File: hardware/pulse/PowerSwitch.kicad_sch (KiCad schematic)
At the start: 22 parts, among them J1801 WAGO 2065-100, J1802 WAGO 2065-100, U1801 BTT6010

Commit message: Refresh
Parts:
- U1801: Rating (none) -> 36V
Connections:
- net +24V-Supply renamed +28V-Supply
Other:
- note added: "100R / Solenoid coil voltage divider Supplies reference voltage to a single channel while the +28V power is switched off."
- note removed: "100R / Solenoid coil voltage divider Supplies reference voltage to a single channel while the +24V power is switched off."
- company: +24V -> Versio Duo
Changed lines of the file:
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@@
 	(title_block
 		(title "Power Switch")
-		(date "2023-01-07")
-		(rev "1")
-		(company "+24V")
-		(comment 1 "Voltage + Current Sense")
+		(date "2026-02-24")
+		(rev "2026-02-24")
+		(company "Versio Duo")
+		(comment 1 "+28V")
+		(comment 2 "Voltage + Current Sense")
 	)
 	(text "Supply Voltage"
@@
 		)
 	)
-	(text "100R / Solenoid coil voltage divider\nSupplies reference voltage to a single channel\nwhile the +24V power is switched off."
+	(text "100R / Solenoid coil voltage divider\nSupplies reference voltage to a single channel\nwhile the +28V power is switched off."
 		(exclude_from_sim no)
 		(at 180.34 149.225 0)
@@
 		)
 	)
-	(label "+24V-Supply"
+	(label "+28V-Supply"
 		(at 177.8 68.58 0)
 		(effects
@@
 		)
 	)
-	(label "+24V-Supply"
+	(label "+28V-Supply"
 		(at 101.6 120.65 0)
 		(effects
@@
 		)
 	)
-	(label "+24V-Supply"
+	(label "+28V-Supply"
 		(at 156.21 76.2 180)
 		(effects
@@
 		)
 	)
-	(label "+24V-Supply"
+	(label "+28V-Supply"
 		(at 128.27 68.58 180)
 		(effects
@@
 		(on_board yes)
 		(dnp no)
-		(property "Reference" "#PWR01805"
+		(property "Reference" "#PWR1805"
 			(at 102.87 90.17 0)
 			(effects
@@
 			(project "pulse"
 				(path "/6c8448b4-b04d-47e1-934e-e40cbe27a7be/ba748654-beb9-4861-aa35-c19e08caaf2e"
-					(reference "#PWR01805")
+					(reference "#PWR1805")
 					(unit 1)
 				)
@@
 		(on_board yes)
 		(dnp no)
-		(property "Reference" "#PWR01804"
+		(property "Reference" "#PWR1804"
 			(at 218.44 87.63 0)
 			(effects
@@
 			(project "pulse"
 				(path "/6c8448b4-b04d-47e1-934e-e40cbe27a7be/ba748654-beb9-4861-aa35-c19e08caaf2e"
-					(reference "#PWR01804")
+					(reference "#PWR1804")
 					(unit 1)
 				)
@@
 		(on_board yes)
 		(dnp no)
-		(property "Reference" "#PWR01802"
+		(property "Reference" "#PWR1802"
 			(at 132.08 87.63 0)
 			(effects
@@
 			(project "pulse"
 				(path "/6c8448b4-b04d-47e1-934e-e40cbe27a7be/ba748654-beb9-4861-aa35-c19e08caaf2e"
-					(reference "#PWR01802")
+					(reference "#PWR1802")
 					(unit 1)
 				)
@@
 		(on_board yes)
 		(dnp no)
-		(property "Reference" "#PWR01817"
+		(property "Reference" "#PWR1817"
 			(at 107.95 147.32 0)
 			(effects
@@
 			(project "pulse"
 				(path "/6c8448b4-b04d-47e1-934e-e40cbe27a7be/ba748654-beb9-4861-aa35-c19e08caaf2e"
-					(reference "#PWR01817")
+					(reference "#PWR1817")
 					(unit 1)
 				)
@@
 		(on_board yes)
 		(dnp no)
-		(property "Reference" "#PWR01809"
+		(property "Reference" "#PWR1809"
 			(at 154.94 132.08 0)
 			(effects
@@
 			(project "pulse"
 				(path "/6c8448b4-b04d-47e1-934e-e40cbe27a7be/ba748654-beb9-4861-aa35-c19e08caaf2e"
-					(reference "#PWR01809")
+					(reference "#PWR1809")
 					(unit 1)
 				)
@@
 		(on_board yes)
 		(dnp no)
-		(property "Reference" "#PWR01811"
+		(property "Reference" "#PWR1811"
 			(at 85.09 137.16 0)
 			(effects
@@
 			(project "pulse"
 				(path "/6c8448b4-b04d-47e1-934e-e40cbe27a7be/ba748654-beb9-4861-aa35-c19e08caaf2e"
-					(reference "#PWR01811")
+					(reference "#PWR1811")
 					(unit 1)
 				)
@@
 		(on_board yes)
 		(dnp no)
-		(property "Reference" "#PWR01814"
+		(property "Reference" "#PWR1814"
 			(at 217.17 137.16 0)
 			(effects
@@
 			(project "pulse"
 				(path "/6c8448b4-b04d-47e1-934e-e40cbe27a7be/ba748654-beb9-4861-aa35-c19e08caaf2e"
-					(reference "#PWR01814")
+					(reference "#PWR1814")
 					(unit 1)
 				)
@@
 		(on_board yes)
 		(dnp no)
-		(property "Reference" "#PWR01807"
+		(property "Reference" "#PWR1807"
 			(at 199.39 124.46 0)
 			(effects
@@
 			(project "pulse"
 				(path "/6c8448b4-b04d-47e1-934e-e40cbe27a7be/ba748654-beb9-4861-aa35-c19e08caaf2e"
-					(reference "#PWR01807")
+					(reference "#PWR1807")
 					(unit 1)
 				)
@@
 		(on_board yes)
 		(dnp no)
-		(property "Reference" "#PWR01815"
+		(property "Reference" "#PWR1815"
 			(at 143.51 135.89 0)
 			(effects
@@
 			(project "pulse"
 				(path "/6c8448b4-b04d-47e1-934e-e40cbe27a7be/ba748654-beb9-4861-aa35-c19e08caaf2e"
-					(reference "#PWR01815")
+					(reference "#PWR1815")
 					(unit 1)
 				)
@@
 		(on_board yes)
 		(dnp no)
-		(property "Reference" "#PWR01801"
+		(property "Reference" "#PWR1801"
 			(at 120.65 87.63 0)
 			(effects
@@
 			(project "pulse"
 				(path "/6c8448b4-b04d-47e1-934e-e40cbe27a7be/ba748654-beb9-4861-aa35-c19e08caaf2e"
-					(reference "#PWR01801")
+					(reference "#PWR1801")
 					(unit 1)
 				)
@@
 			)
 		)
-		(property "Description" "Infineon Smart High Sde Switches PROFET™+ 24V"
+		(property "Description" "Infineon Smart High Side Switches PROFET™+ 24V"
 			(at 127 128.27 0)
 			(effects
@@
 			)
 		)
+		(property "Rating" "36V"
+			(at 127 179.07 0)
+			(effects
+				(font
+					(size 1.27 1.27)
+				)
+				(hide yes)
+			)
+		)
 		(pin "1"
 		)
@@
 		(on_board yes)
 		(dnp no)
-		(property "Reference" "#PWR01806"
+		(property "Reference" "#PWR1806"
 			(at 167.64 124.46 0)
 			(effects
@@
 			(project "pulse"
 				(path "/6c8448b4-b04d-47e1-934e-e40cbe27a7be/ba748654-beb9-4861-aa35-c19e08caaf2e"
-					(reference "#PWR01806")
+					(reference "#PWR1806")
 					(unit 1)
 				)
@@
 		(on_board yes)
 		(dnp no)
-		(property "Reference" "#PWR01813"
+		(property "Reference" "#PWR1813"
 			(at 199.39 127 0)
 			(effects
@@
 			(project "pulse"
 				(path "/6c8448b4-b04d-47e1-934e-e40cbe27a7be/ba748654-beb9-4861-aa35-c19e08caaf2e"
-					(reference "#PWR01813")
+					(reference "#PWR1813")
 					(unit 1)
 				)
@@
 		(on_board yes)
 		(dnp no)
-		(property "Reference" "#PWR01818"
+		(property "Reference" "#PWR1818"
 			(at 116.84 147.32 0)
 			(effects
@@
 			(project "pulse"
 				(path "/6c8448b4-b04d-47e1-934e-e40cbe27a7be/ba748654-beb9-4861-aa35-c19e08caaf2e"
-					(reference "#PWR01818")
+					(reference "#PWR1818")
 					(unit 1)
 				)
@@
 		(on_board yes)
 		(dnp no)
-		(property "Reference" "#PWR01803"
+		(property "Reference" "#PWR1803"
 			(at 193.04 87.63 0)
 			(effects
@@
 			(project "pulse"
 				(path "/6c8448b4-b04d-47e1-934e-e40cbe27a7be/ba748654-beb9-4861-aa35-c19e08caaf2e"
-					(reference "#PWR01803")
+					(reference "#PWR1803")
 					(unit 1)
 				)
@@
 		(on_board yes)
 		(dnp no)
-		(property "Reference" "#PWR01810"
+		(property "Reference" "#PWR1810"
 			(at 167.64 132.08 0)
 			(effects
@@
 			(project "pulse"
 				(path "/6c8448b4-b04d-47e1-934e-e40cbe27a7be/ba748654-beb9-4861-aa35-c19e08caaf2e"
-					(reference "#PWR01810")
+					(reference "#PWR1810")
 					(unit 1)
 				)
@@
 		(on_board yes)
 		(dnp no)
-		(property "Reference" "#FLG01801"
+		(property "Reference" "#FLG1801"
 			(at 113.03 66.675 0)
 			(effects
@@
 			(project "pulse"
 				(path "/6c8448b4-b04d-47e1-934e-e40cbe27a7be/ba748654-beb9-4861-aa35-c19e08caaf2e"
-					(reference "#FLG01801")
+					(reference "#FLG1801")
 					(unit 1)
 				)
@@
 		(on_board yes)
 		(dnp no)
-		(property "Reference" "#PWR01808"
+		(property "Reference" "#PWR1808"
 			(at 142.24 132.08 0)
 			(effects
@@
 			(project "pulse"
 				(path "/6c8448b4-b04d-47e1-934e-e40cbe27a7be/ba748654-beb9-4861-aa35-c19e08caaf2e"
-					(reference "#PWR01808")
+					(reference "#PWR1808")
 					(unit 1)
 				)
@@
 		(on_board yes)
 		(dnp no)
-		(property "Reference" "#PWR01816"
+		(property "Reference" "#PWR1816"
 			(at 85.09 147.32 0)
 			(effects
@@
 			(project "pulse"
 				(path "/6c8448b4-b04d-47e1-934e-e40cbe27a7be/ba748654-beb9-4861-aa35-c19e08caaf2e"
-					(reference "#PWR01816")
+					(reference "#PWR1816")
 					(unit 1)
 				)
@@
 		(on_board yes)
 		(dnp no)
-		(property "Reference" "#PWR01812"
+		(property "Reference" "#PWR1812"
 			(at 120.65 130.81 0)
 			(effects
@@
 			(project "pulse"
 				(path "/6c8448b4-b04d-47e1-934e-e40cbe27a7be/ba748654-beb9-4861-aa35-c19e08caaf2e"
-					(reference "#PWR01812")
+					(reference "#PWR1812")
 					(unit 1)
 				)

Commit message: Refresh
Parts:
- C1801: Mouser 810-CNA6P1X7R1H106K2 -> 810-CNC6P1X7R1H106K2; Product CNA6P1X7R1H106K250AE -> CNC6P1X7R1H106K250AE
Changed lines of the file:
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@@
 			)
 		)
-		(property "Mouser" "810-CNA6P1X7R1H106K2"
+		(property "Mouser" "810-CNC6P1X7R1H106K2"
 			(at 120.65 95.25 0)
 			(show_name yes)
@@
 			)
 		)
-		(property "Product" "CNA6P1X7R1H106K250AE"
+		(property "Product" "CNC6P1X7R1H106K250AE"
 			(at 120.65 96.52 0)
 			(effects

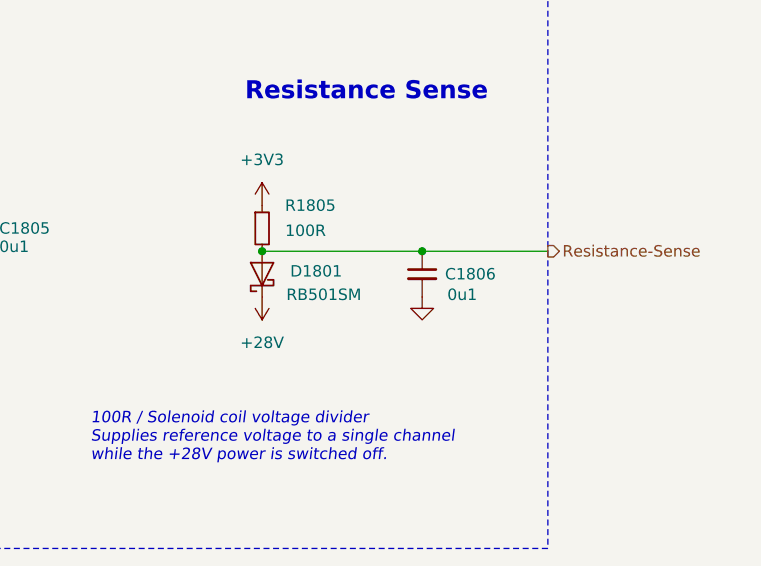
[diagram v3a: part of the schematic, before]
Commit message: Replace diode
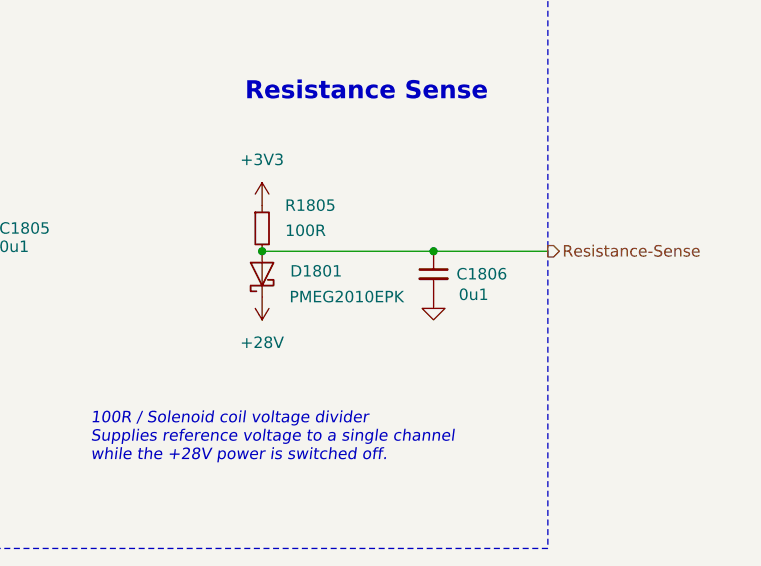
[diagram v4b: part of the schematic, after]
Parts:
- D1801: value RB501SM -> PMEG2010EPK; footprint V2_Diode_SMD:D_SOD-523 -> V2_Diode_SMD:D_SOD-1608; symbol V2_Diode:RB501SM -> V2_Diode:PMEG2010EPK; Manufacturer ROHM Semiconductor -> Nexperia; Mouser 755-RB501SM-30FHT2R -> 771-PMEG2010EPK; Product RB501SM-30FHT2R -> PMEG2010EPK; Rating (none) -> 20V
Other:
- title: Power Switch -> V2 pulse
- moved on the sheet: C1806

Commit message: Update
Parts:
- C1801, C1802, C1803, C1804, C1805, C1806, C1807: Id (none) -> Capacitor:${SYMBOL_NAME}
- D1801, TVS1801: Id (none) -> Diode:${SYMBOL_NAME}
- J1801, J1802: Id (none) -> WAGO:${SYMBOL_NAME}
- R1801, R1802, R1803, R1804, R1805, R1806, R1807, R1808, R1809, R1810: Id (none) -> Resistor:${SYMBOL_NAME}
- U1801: Id (none) -> PowerSwitch:${SYMBOL_NAME}

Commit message: Update
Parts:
- J1801, J1802: Rating (none) -> 9A
- renumbered C1807 to C1801, C1801 to C1802, C1802 to C1803, C1803 to C1806, C1806 to C1807, R1807 to R1801, R1806 to R1802, R1808 to R1803, R1809 to R1804, R1810 to R1805, R1804 to R1806, R1801 to R1807, R1803 to R1808, R1805 to R1809, R1802 to R1810

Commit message: Good Bye Imperial
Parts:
- C1801, C1803, C1804, C1805, C1806, C1807: footprint V2_Capacitor_SMD:C_0603 -> V2_Capacitor_SMD:C_1608; symbol V2_Capacitor:0603_0u1 -> V2_Capacitor:1608_0u1
- C1802: footprint V2_Capacitor_SMD:C_1210 -> V2_Capacitor_SMD:C_3225; symbol V2_Capacitor:1210_10u -> V2_Capacitor:3225_10u
- R1801, R1806, R1807: footprint V2_Resistor_SMD:R_0603 -> V2_Resistor_SMD:R_1608; symbol V2_Resistor:0603_100k -> V2_Resistor:1608_100k
- R1802, R1803, R1808, R1810: footprint V2_Resistor_SMD:R_0603 -> V2_Resistor_SMD:R_1608; symbol V2_Resistor:0603_10k -> V2_Resistor:1608_10k
- R1804, R1805: footprint V2_Resistor_SMD:R_0603 -> V2_Resistor_SMD:R_1608; symbol V2_Resistor:0603_2k7 -> V2_Resistor:1608_2k7
- R1809: footprint V2_Resistor_SMD:R_0603 -> V2_Resistor_SMD:R_1608; symbol V2_Resistor:0603_100R -> V2_Resistor:1608_100R
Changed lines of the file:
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@@
 	)
 	(symbol
-		(lib_id "V2_Capacitor:1210_10u")
+		(lib_id "V2_Capacitor:3225_10u")
 		(at 120.65 78.74 0)
 		(unit 1)
@@
 			)
 		)
-		(property "Footprint" "V2_Capacitor_SMD:C_1210"
+		(property "Footprint" "V2_Capacitor_SMD:C_3225"
 			(at 120.65 95.758 0)
 			(hide yes)
@@
 	)
 	(symbol
-		(lib_id "V2_Resistor:0603_10k")
+		(lib_id "V2_Resistor:1608_10k")
 		(at 92.71 125.73 270)
 		(unit 1)
@@
 			)
 		)
-		(property "Footprint" "V2_Resistor_SMD:R_0603"
+		(property "Footprint" "V2_Resistor_SMD:R_1608"
 			(at 76.962 125.73 0)
 			(hide yes)
@@
 	)
 	(symbol
-		(lib_id "V2_Resistor:0603_10k")
+		(lib_id "V2_Resistor:1608_10k")
 		(at 92.71 135.89 90)
 		(unit 1)
@@
 			)
 		)
-		(property "Footprint" "V2_Resistor_SMD:R_0603"
+		(property "Footprint" "V2_Resistor_SMD:R_1608"
 			(at 108.458 135.89 0)
 			(hide yes)
@@
 	)
 	(symbol
-		(lib_id "V2_Resistor:0603_10k")
+		(lib_id "V2_Resistor:1608_10k")
 		(at 208.28 76.2 90)
 		(unit 1)
@@
 			)
 		)
-		(property "Footprint" "V2_Resistor_SMD:R_0603"
+		(property "Footprint" "V2_Resistor_SMD:R_1608"
 			(at 224.028 76.2 0)
 			(hide yes)
@@
 	)
 	(symbol
-		(lib_id "V2_Resistor:0603_2k7")
+		(lib_id "V2_Resistor:1608_2k7")
 		(at 107.95 138.43 0)
 		(unit 1)
@@
 			)
 		)
-		(property "Footprint" "V2_Resistor_SMD:R_0603"
+		(property "Footprint" "V2_Resistor_SMD:R_1608"
 			(at 107.95 154.178 0)
 			(hide yes)
@@
 	)
 	(symbol
-		(lib_id "V2_Resistor:0603_10k")
+		(lib_id "V2_Resistor:1608_10k")
 		(at 193.04 78.74 0)
 		(unit 1)
@@
 			)
 		)
-		(property "Footprint" "V2_Resistor_SMD:R_0603"
+		(property "Footprint" "V2_Resistor_SMD:R_1608"
 			(at 193.04 94.488 0)
 			(hide yes)
@@
 	)
 	(symbol
-		(lib_id "V2_Resistor:0603_100k")
+		(lib_id "V2_Resistor:1608_100k")
 		(at 193.04 73.66 0)
 		(unit 1)
@@
 			)
 		)
-		(property "Footprint" "V2_Resistor_SMD:R_0603"
+		(property "Footprint" "V2_Resistor_SMD:R_1608"
 			(at 193.04 89.408 0)
 			(hide yes)
@@
 	)
 	(symbol
-		(lib_id "V2_Capacitor:0603_0u1")
+		(lib_id "V2_Capacitor:1608_0u1")
 		(at 154.94 123.19 0)
 		(unit 1)
@@
 			)
 		)
-		(property "Footprint" "V2_Capacitor_SMD:C_0603"
+		(property "Footprint" "V2_Capacitor_SMD:C_1608"
 			(at 154.94 140.208 0)
 			(hide yes)
@@
 	)
 	(symbol
-		(lib_id "V2_Resistor:0603_100k")
+		(lib_id "V2_Resistor:1608_100k")
 		(at 85.09 128.27 180)
 		(unit 1)
@@
 			)
 		)
-		(property "Footprint" "V2_Resistor_SMD:R_0603"
+		(property "Footprint" "V2_Resistor_SMD:R_1608"
 			(at 85.09 112.522 0)
 			(hide yes)
@@
 	)
 	(symbol
-		(lib_id "V2_Resistor:0603_100k")
+		(lib_id "V2_Resistor:1608_100k")
 		(at 142.24 123.19 0)
 		(unit 1)
@@
 			)
 		)
-		(property "Footprint" "V2_Resistor_SMD:R_0603"
+		(property "Footprint" "V2_Resistor_SMD:R_1608"
 			(at 142.24 138.938 0)
 			(hide yes)
@@
 	)
 	(symbol
-		(lib_id "V2_Resistor:0603_100R")
+		(lib_id "V2_Resistor:1608_100R")
 		(at 199.39 123.19 0)
 		(unit 1)
@@
 			)
 		)
-		(property "Footprint" "V2_Resistor_SMD:R_0603"
+		(property "Footprint" "V2_Resistor_SMD:R_1608"
 			(at 199.39 138.938 0)
 			(hide yes)
@@
 	)
 	(symbol
-		(lib_id "V2_Capacitor:0603_0u1")
+		(lib_id "V2_Capacitor:1608_0u1")
 		(at 132.08 78.74 0)
 		(unit 1)
@@
 			)
 		)
-		(property "Footprint" "V2_Capacitor_SMD:C_0603"
+		(property "Footprint" "V2_Capacitor_SMD:C_1608"
 			(at 132.08 95.758 0)
 			(hide yes)
@@
 	)
 	(symbol
-		(lib_id "V2_Resistor:0603_2k7")
+		(lib_id "V2_Resistor:1608_2k7")
 		(at 116.84 138.43 0)
 		(unit 1)
@@
 			)
 		)
-		(property "Footprint" "V2_Resistor_SMD:R_0603"
+		(property "Footprint" "V2_Resistor_SMD:R_1608"
 			(at 116.84 154.178 0)
 			(hide yes)
@@
 	)
 	(symbol
-		(lib_id "V2_Capacitor:0603_0u1")
+		(lib_id "V2_Capacitor:1608_0u1")
 		(at 85.09 138.43 0)
 		(unit 1)
@@
 			)
 		)
-		(property "Footprint" "V2_Capacitor_SMD:C_0603"
+		(property "Footprint" "V2_Capacitor_SMD:C_1608"
 			(at 85.09 155.448 0)
 			(hide yes)
@@
 	)
 	(symbol
-		(lib_id "V2_Capacitor:0603_0u1")
+		(lib_id "V2_Capacitor:1608_0u1")
 		(at 218.44 128.27 0)
 		(unit 1)
@@
 			)
 		)
-		(property "Footprint" "V2_Capacitor_SMD:C_0603"
+		(property "Footprint" "V2_Capacitor_SMD:C_1608"
 			(at 218.44 145.288 0)
 			(hide yes)
@@
 	)
 	(symbol
-		(lib_id "V2_Capacitor:0603_0u1")
+		(lib_id "V2_Capacitor:1608_0u1")
 		(at 167.64 123.19 0)
 		(unit 1)
@@
 			)
 		)
-		(property "Footprint" "V2_Capacitor_SMD:C_0603"
+		(property "Footprint" "V2_Capacitor_SMD:C_1608"
 			(at 167.64 140.208 0)
 			(hide yes)
@@
 	)
 	(symbol
-		(lib_id "V2_Capacitor:0603_0u1")
+		(lib_id "V2_Capacitor:1608_0u1")
 		(at 218.44 78.74 0)
 		(unit 1)
@@
 			)
 		)
-		(property "Footprint" "V2_Capacitor_SMD:C_0603"
+		(property "Footprint" "V2_Capacitor_SMD:C_1608"
 			(at 218.44 95.758 0)
 			(hide yes)
